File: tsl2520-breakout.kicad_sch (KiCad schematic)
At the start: 13 parts, among them J1 Conn_01x08, U1 TSL2585, U2 MIC5365-1.8YC5

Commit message: Rename project files and identifiers
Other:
- title: TSL2585 Sensor Breakout Board -> TSL2520 Sensor Breakout Board
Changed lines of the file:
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@@
   (paper "USLetter")
   (title_block
-    (title "TSL2585 Sensor Breakout Board")
+    (title "TSL2520 Sensor Breakout Board")
     (date "2023-11-27")
     (rev "A")
@@
         )
       )
-      (project "tsl2585-breakout"
+      (project "tsl2520-breakout"
         (path "/3f3ab8a6-b03e-4a96-9558-b31e20a6d8cc"
           (reference "R1") (unit 1)
@@
         )
       )
-      (project "tsl2585-breakout"
+      (project "tsl2520-breakout"
         (path "/3f3ab8a6-b03e-4a96-9558-b31e20a6d8cc"
           (reference "#PWR05") (unit 1)
@@
         )
       )
-      (project "tsl2585-breakout"
+      (project "tsl2520-breakout"
         (path "/3f3ab8a6-b03e-4a96-9558-b31e20a6d8cc"
           (reference "U1") (unit 1)
@@
         )
       )
-      (project "tsl2585-breakout"
+      (project "tsl2520-breakout"
         (path "/3f3ab8a6-b03e-4a96-9558-b31e20a6d8cc"
           (reference "#PWR02") (unit 1)
@@
     (pin "1")
     (instances
-      (project "tsl2585-breakout"
+      (project "tsl2520-breakout"
         (path "/3f3ab8a6-b03e-4a96-9558-b31e20a6d8cc"
           (reference "#PWR06") (unit 1)
@@
         )
       )
-      (project "tsl2585-breakout"
+      (project "tsl2520-breakout"
         (path "/3f3ab8a6-b03e-4a96-9558-b31e20a6d8cc"
           (reference "#PWR01") (unit 1)
@@
         )
       )
-      (project "tsl2585-breakout"
+      (project "tsl2520-breakout"
         (path "/3f3ab8a6-b03e-4a96-9558-b31e20a6d8cc"
           (reference "C2") (unit 1)
@@
     )
     (instances
-      (project "tsl2585-breakout"
+      (project "tsl2520-breakout"
         (path "/3f3ab8a6-b03e-4a96-9558-b31e20a6d8cc"
           (reference "H2") (unit 1)
@@
         )
       )
-      (project "tsl2585-breakout"
+      (project "tsl2520-breakout"
         (path "/3f3ab8a6-b03e-4a96-9558-b31e20a6d8cc"
           (reference "R4") (unit 1)
@@
     )
     (instances
-      (project "tsl2585-breakout"
+      (project "tsl2520-breakout"
         (path "/3f3ab8a6-b03e-4a96-9558-b31e20a6d8cc"
           (reference "H1") (unit 1)
@@
         )
       )
-      (project "tsl2585-breakout"
+      (project "tsl2520-breakout"
         (path "/3f3ab8a6-b03e-4a96-9558-b31e20a6d8cc"
           (reference "R3") (unit 1)
@@
         )
       )
-      (project "tsl2585-breakout"
+      (project "tsl2520-breakout"
         (path "/3f3ab8a6-b03e-4a96-9558-b31e20a6d8cc"
           (reference "#FLG03") (unit 1)
@@
         )
       )
-      (project "tsl2585-breakout"
+      (project "tsl2520-breakout"
         (path "/3f3ab8a6-b03e-4a96-9558-b31e20a6d8cc"
           (reference "C1") (unit 1)
@@
         )
       )
-      (project "tsl2585-breakout"
+      (project "tsl2520-breakout"
         (path "/3f3ab8a6-b03e-4a96-9558-b31e20a6d8cc"
           (reference "#PWR04") (unit 1)
@@
         )
       )
-      (project "tsl2585-breakout"
+      (project "tsl2520-breakout"
         (path "/3f3ab8a6-b03e-4a96-9558-b31e20a6d8cc"
           (reference "#PWR09") (unit 1)
@@
         )
       )
-      (project "tsl2585-breakout"
+      (project "tsl2520-breakout"
         (path "/3f3ab8a6-b03e-4a96-9558-b31e20a6d8cc"
           (reference "#FLG02") (unit 1)
@@
     (pin "1")
     (instances
-      (project "tsl2585-breakout"
+      (project "tsl2520-breakout"
         (path "/3f3ab8a6-b03e-4a96-9558-b31e20a6d8cc"
           (reference "#PWR08") (unit 1)
@@
     (pin "3")
     (instances
-      (project "tsl2585-breakout"
+      (project "tsl2520-breakout"
         (path "/3f3ab8a6-b03e-4a96-9558-b31e20a6d8cc"
           (reference "J1") (unit 1)
@@
     (pin "1")
     (instances
-      (project "tsl2585-breakout"
+      (project "tsl2520-breakout"
         (path "/3f3ab8a6-b03e-4a96-9558-b31e20a6d8cc"
           (reference "U2") (unit 1)
@@
         )
       )
-      (project "tsl2585-breakout"
+      (project "tsl2520-breakout"
         (path "/3f3ab8a6-b03e-4a96-9558-b31e20a6d8cc"
           (reference "#PWR07") (unit 1)
@@
         )
       )
-      (project "tsl2585-breakout"
+      (project "tsl2520-breakout"
         (path "/3f3ab8a6-b03e-4a96-9558-b31e20a6d8cc"
           (reference "C3") (unit 1)
@@
         )
       )
-      (project "tsl2585-breakout"
+      (project "tsl2520-breakout"
         (path "/3f3ab8a6-b03e-4a96-9558-b31e20a6d8cc"
           (reference "C4") (unit 1)
@@
         )
       )
-      (project "tsl2585-breakout"
+      (project "tsl2520-breakout"
         (path "/3f3ab8a6-b03e-4a96-9558-b31e20a6d8cc"
           (reference "#FLG01") (unit 1)
@@
         )
       )
-      (project "tsl2585-breakout"
+      (project "tsl2520-breakout"
         (path "/3f3ab8a6-b03e-4a96-9558-b31e20a6d8cc"
           (reference "#PWR03") (unit 1)
@@
         )
       )
-      (project "tsl2585-breakout"
+      (project "tsl2520-breakout"
         (path "/3f3ab8a6-b03e-4a96-9558-b31e20a6d8cc"
           (reference "R2") (unit 1)

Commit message: Update symbol, schematic, and PCB layout
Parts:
- U1: value TSL2585 -> TSL2520; symbol AMS_Sensor_Optical:TSL2585 -> AMS_Sensor_Optical:TSL2520; Manufacturer PN TSL25853PM -> TSL25203M; Supplier PN 4991-TSL25853PMCT-ND -> 4991-TSL25203MCT-ND
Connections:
- net SENSOR_INT: now also U1.1 (INT); no longer U1.5 (INT)
- net SENSOR_SDA: now also U1.5 (SDA); no longer U1.6 (SDA)
- net SENSOR_VSYNC: now also U1.6 (VSYNC/GPIO); no longer U1.2 (VSYNC/GPIO)
- net at C2.1, R1.1: now also U1.2 (VDD); no longer U1.1 (VDD)
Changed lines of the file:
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@@
     )
   )
-  (symbol (lib_id "AMS_Sensor_Optical:TSL2585") (at 33.02 53.34 0) (unit 1)
+  (symbol (lib_id "AMS_Sensor_Optical:TSL2520") (at 33.02 53.34 0) (unit 1)
     (in_bom yes) (on_board yes) (dnp no)
     (property "Reference" "U1" (at 26.67 41.91 0)
       (effects (font (size 1.27 1.27)) (justify right))
     )
-    (property "Value" "TSL2585" (at 42.545 64.77 0)
+    (property "Value" "TSL2520" (at 42.545 64.77 0)
       (effects (font (size 1.27 1.27)) (justify right))
     )
-    (property "Footprint" "lib_fp:AMS_TSL2585_OLGA-6_2x1mm_P0.65mm" (at 34.29 64.77 0)
+    (property "Footprint" "lib_fp:AMS_TSL2585_OLGA-6_2x1mm_P0.65mm" (at 33.02 76.835 0)
       (effects (font (size 1.27 1.27)) hide)
     )
-    (property "Datasheet" "https://ams.com/documents/20143/6148289/TSL2585_DS001043_4-00.pdf" (at 33.02 77.47 0)
+    (property "Datasheet" "https://ams.com/documents/20143/4410897/TSL2520_DS001068_3-00.pdf" (at 33.02 79.375 0)
       (effects (font (size 1.27 1.27)) hide)
     )
@@
       (effects (font (size 1.27 1.27)) hide)
     )
-    (property "Manufacturer PN" "TSL25853PM" (at 33.02 53.34 0)
+    (property "Manufacturer PN" "TSL25203M" (at 33.02 53.34 0)
       (effects (font (size 1.27 1.27)) hide)
     )
@@
       (effects (font (size 1.27 1.27)) hide)
     )
-    (property "Supplier PN" "4991-TSL25853PMCT-ND" (at 33.02 53.34 0)
+    (property "Supplier PN" "4991-TSL25203MCT-ND" (at 33.02 53.34 0)
       (effects (font (size 1.27 1.27)) hide)
     )

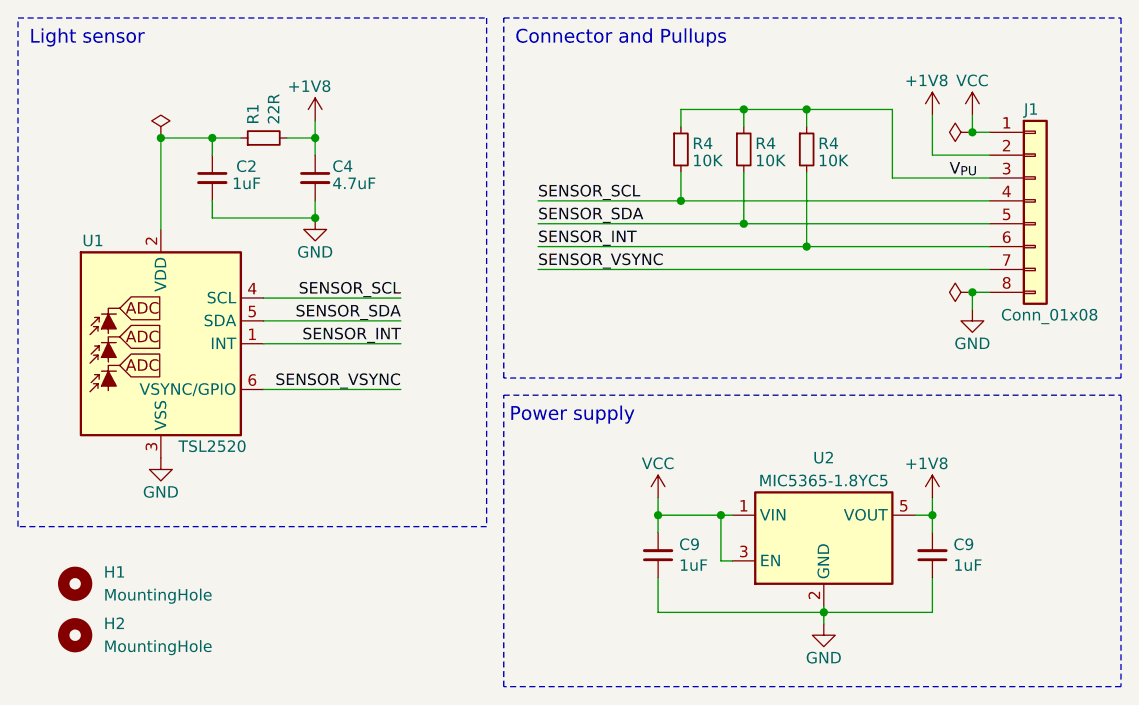
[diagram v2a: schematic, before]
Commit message: Update breakout board design
Changes for KiCad v9 update and various silkscreen changes
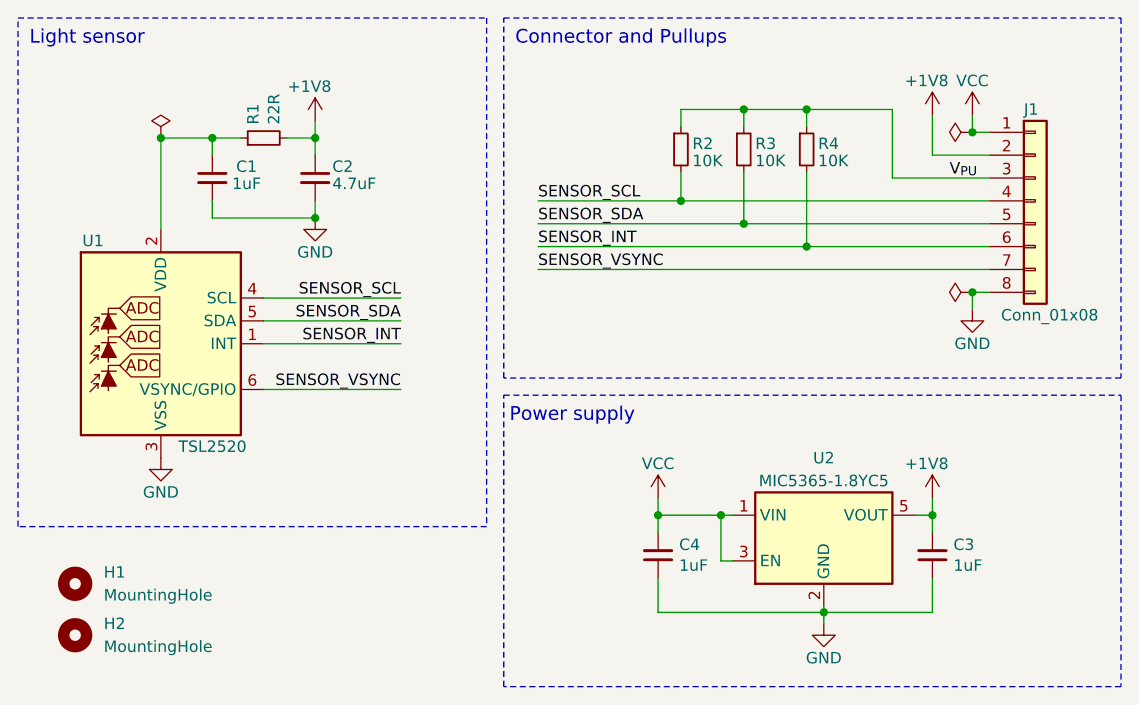
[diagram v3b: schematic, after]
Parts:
- renumbered C2 to C1, C4 to C2, C9 to C3, C9 to C4, R4 to R2, R4 to R3
